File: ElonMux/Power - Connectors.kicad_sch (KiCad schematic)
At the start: 8 parts, among them J501 XT60PW-M, J502 XT60PW-F, J503 XT60PW-M, J504 XT60PW-F

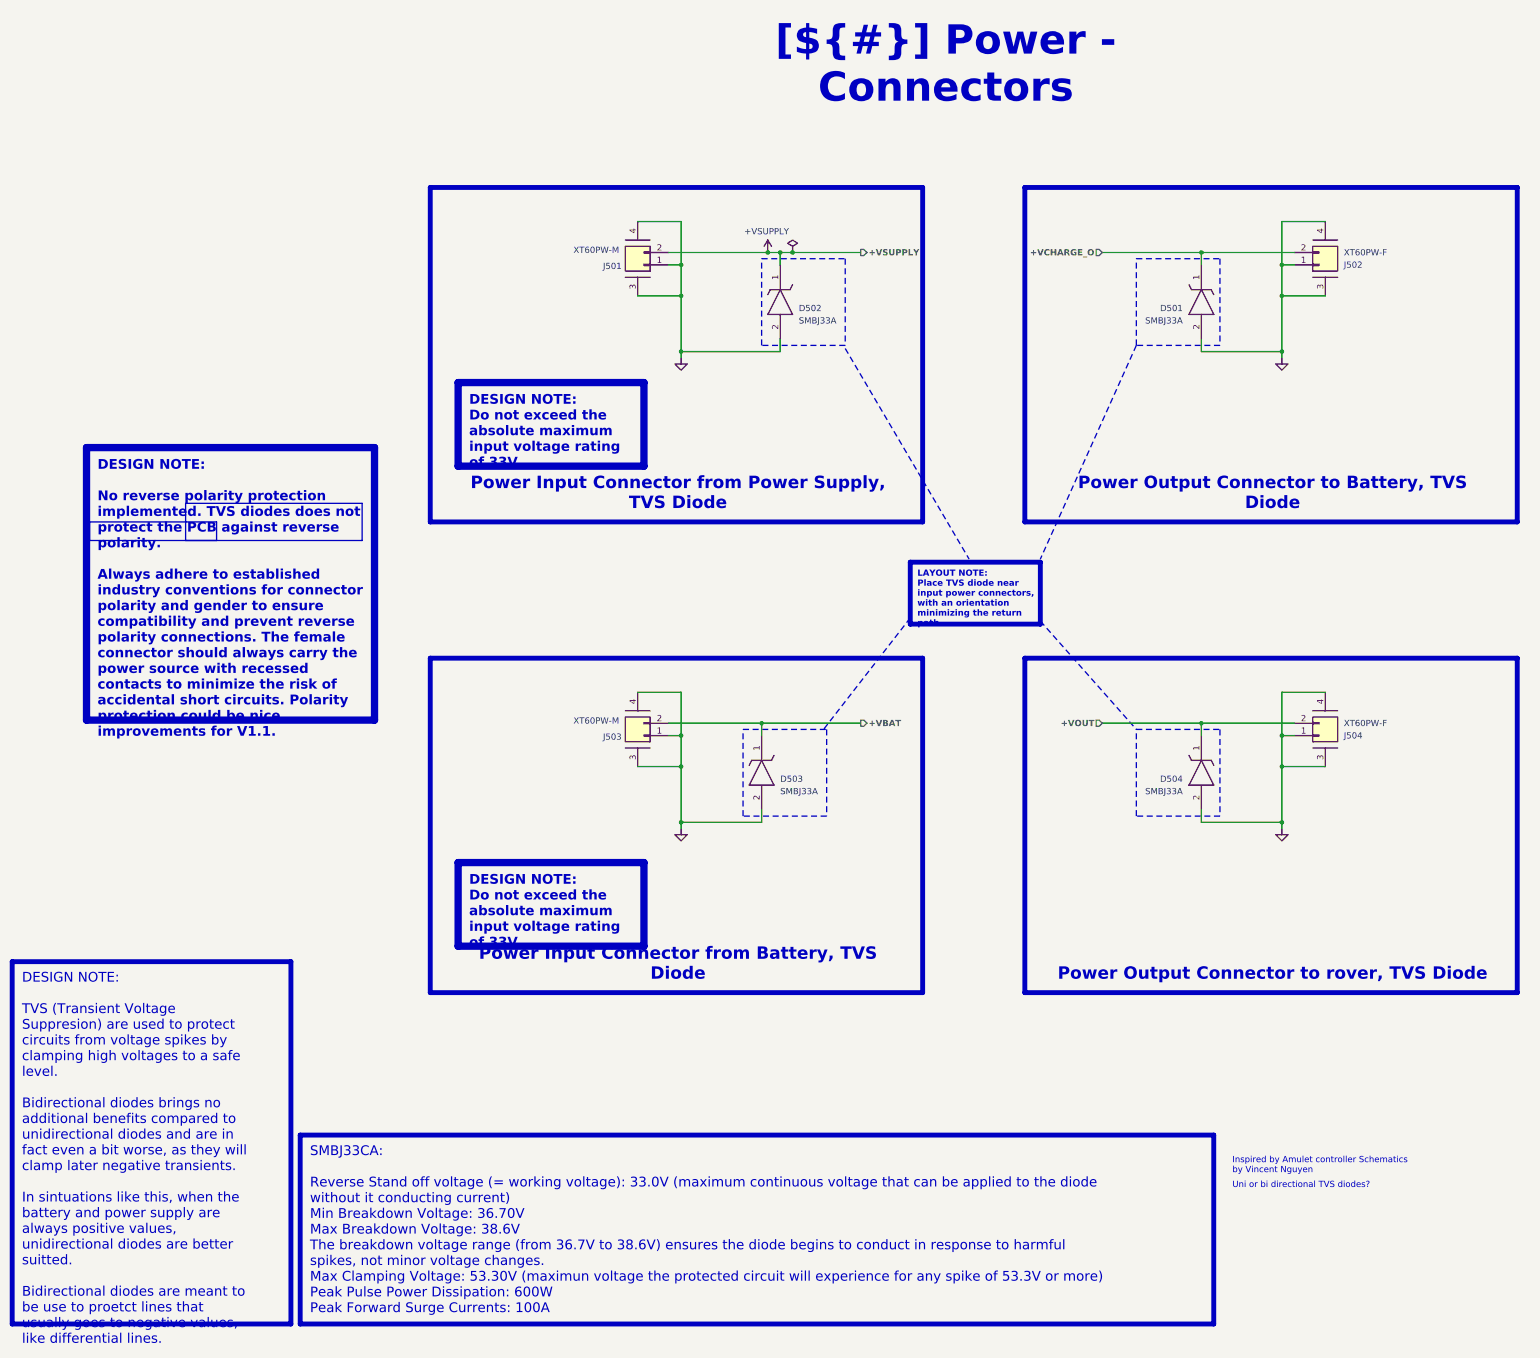
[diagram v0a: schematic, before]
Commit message: Done with changes of v1.1, need to final check and order
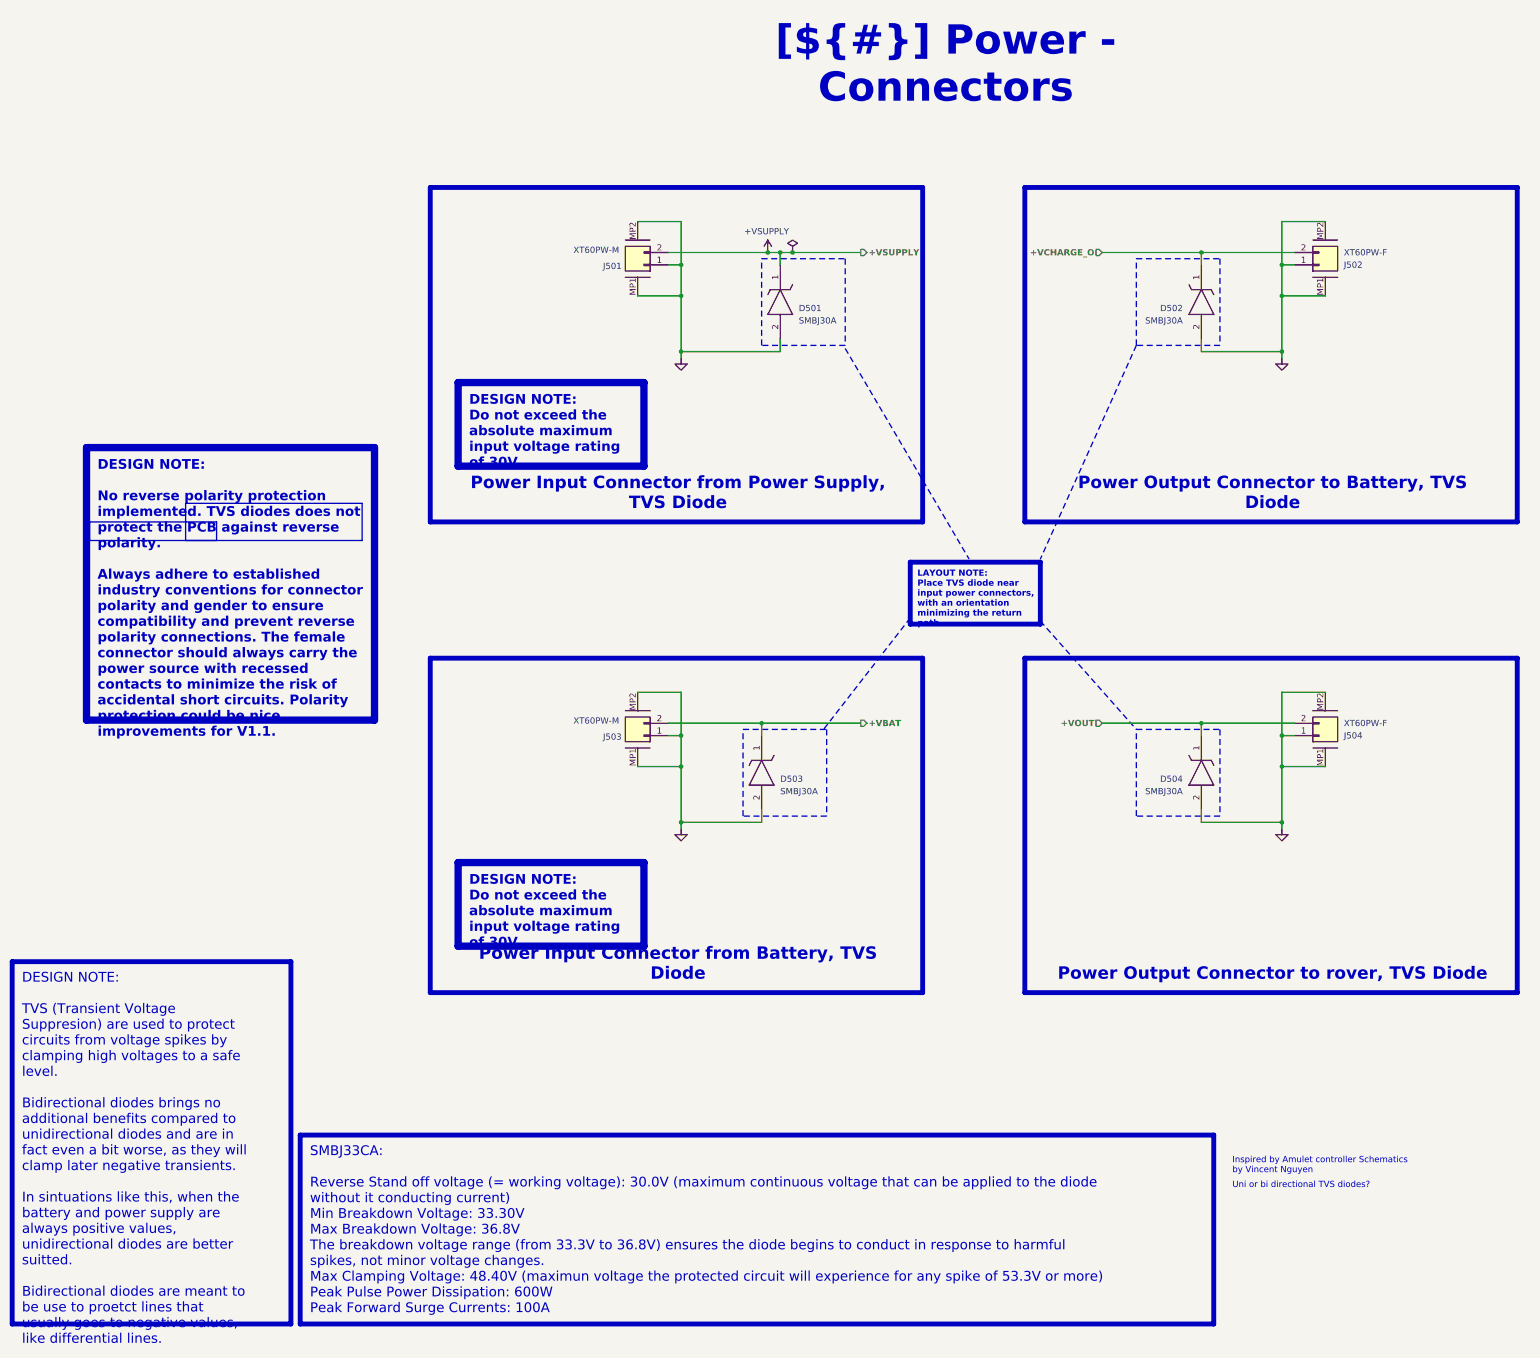
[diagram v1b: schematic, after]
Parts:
- removed D501: SMBJ33A, DIOM5436X244N, symbol Charge_Manager_SYM:SMBJ30CA
- added D502: SMBJ30A, Charge_Manager_FP:DIOM5436X244N, symbol Charge_Manager_SYM:SMBJ30CA
- D501: renamed from D502; value SMBJ33A -> SMBJ30A; footprint DIOM5436X244N -> Charge_Manager_FP:DIOM5436X244N; Manufacturer Part Number SMBJ33A -> SMBJ30A; Supplier Part Number 78-SMBJ33A -> 576-SMBJ30A
- D503, D504: value SMBJ33A -> SMBJ30A; footprint DIOM5436X244N -> Charge_Manager_FP:DIOM5436X244N; Manufacturer Part Number SMBJ33A -> SMBJ30A; Supplier Part Number 78-SMBJ33A -> 576-SMBJ30A
- J501, J502, J503, J504: symbol 0_connectors:Conn_01x02_Mounting -> Charge_Manager_SYM:Conn_01x02_Mounting
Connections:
- net +VCHARGE_O: now also D502.1
- net GND: now also J501.MP1, J501.MP2, J502.MP1, J502.MP2, J503.MP1, J503.MP2, J504.MP1, J504.MP2, D502.2; no longer J501.3 (MP1), J501.4 (MP2), J502.3 (MP1), J502.4 (MP2), J503.3 (MP1), J503.4 (MP2), J504.3 (MP1), J504.4 (MP2)
